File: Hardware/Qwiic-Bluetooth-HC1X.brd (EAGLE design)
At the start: 25.4 x 25.4 mm, 55 parts, among them J1 ISP, J2 Qwiic-L, J3 Qwiic-R, J4 I2C, J5 PIO, U1 ATTiny85-Arduino, U2 HM-17

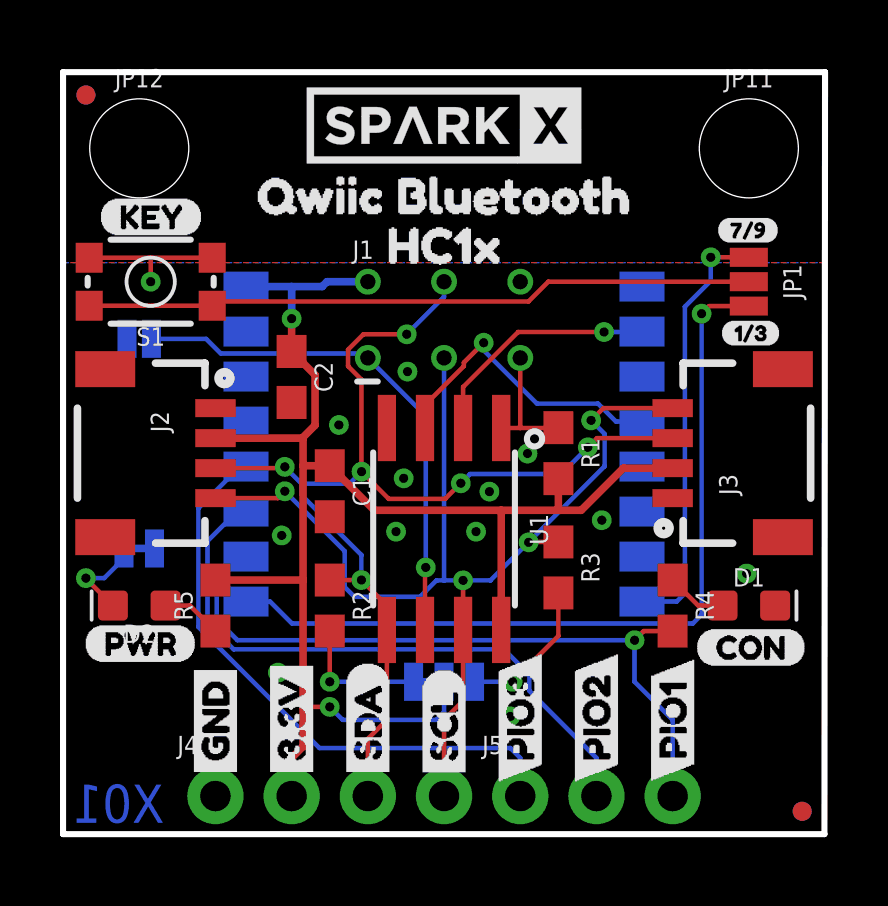
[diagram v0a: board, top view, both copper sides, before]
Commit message: Adding decoupling, fixing silk.
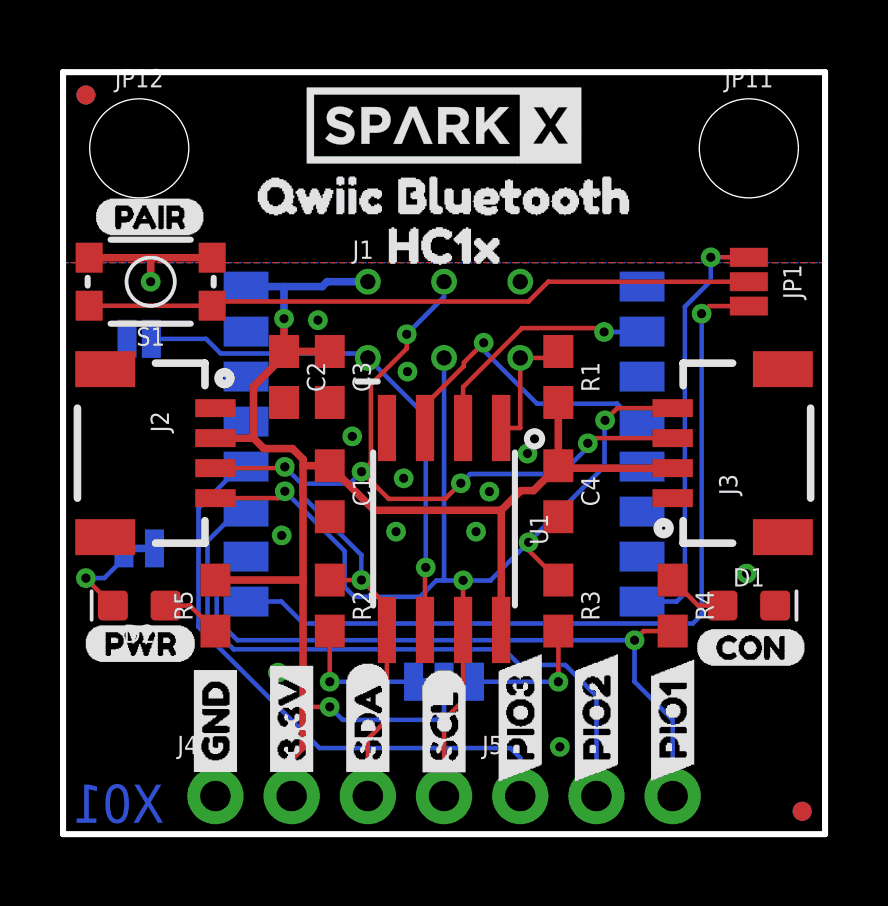
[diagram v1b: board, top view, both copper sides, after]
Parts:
- removed U$12: (no value), Qwiic-Bluetooth-HC1x:KEY6
- removed U$24: (no value), Qwiic-Bluetooth-HC1x:7#915
- added C3: 4.7uF, SparkFun-Capacitors:0603
- added C4: 10uF, SparkFun-Capacitors:0603
- JP3: value (none) -> I2C; device SparkFun-Jumpers:SMT-JUMPER_3_2-NC_TRACE_SILK -> SparkFun-Jumpers:SMT-JUMPER_3_2-NC_TRACE_NO-SILK
- JP4: device SparkFun-Jumpers:SMT-JUMPER_2_NC_TRACE_SILK -> SparkFun-Jumpers:SMT-JUMPER_2_NC_TRACE_NO-SILK
- U$23: device Qwiic-Bluetooth-HC1x:1#314 -> Qwiic-Bluetooth-HC1x:PAIR15
- moved U$23 21.2 mm to (1.02, 20.6)
- moved R1 2.54 mm to (16.5, 15.2)
- moved R3 1.27 mm to (16.5, 7.62)
- moved LOGO2 0.46 mm to (22.9, 12.7), turned to 90 degrees
- moved U$13 0.38 mm to (4.38, 8.13)
- moved U$20 0.38 mm to (14.2, 3.68)
- moved C2 0.25 mm to (7.37, 15.2)
- moved U$19 0.13 mm to (4.38, 15.1)
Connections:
- net PIO1 renamed PIO1/LED
- net 3.3V: now also C3.1, C4.1
- net GND: now also C3.2, C4.2
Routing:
- net 3.3V: track 53.0 -> 54.7 mm
- net SDA: track 39.5 -> 38.3 mm
- net PIO2: track 20.8 -> 21.7 mm

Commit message: Fixing HM-17 pinout, and revising layout to x02
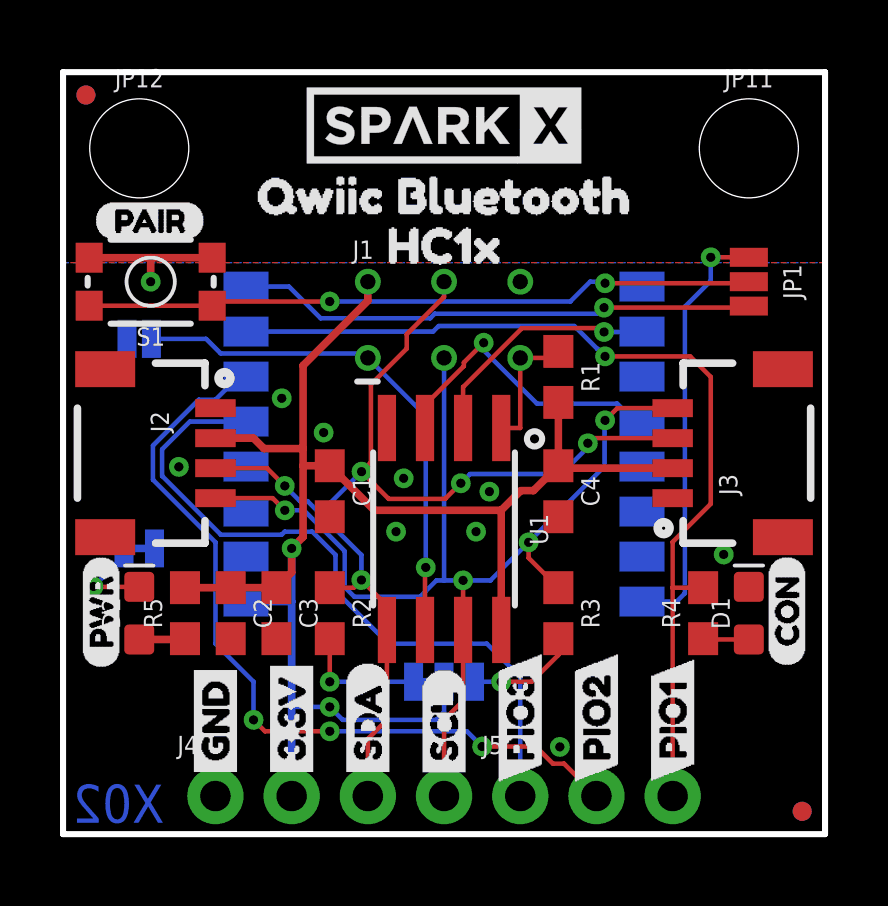
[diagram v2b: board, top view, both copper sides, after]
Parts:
- LOGO2: value SPARKX-LOGO3 -> SPARKX-LOGO4; device SparkX:SPARKX-SMALL -> SparkX:SPARKX-MEDIUM
- moved C3 8.07 mm to (7.11, 7.37)
- moved C2 8.07 mm to (5.59, 7.37)
- moved U$17 3.11 mm to (24.1, 5.59), turned to 90 degrees
- moved R5 1.05 mm to (4.06, 7.37)
- moved R4 1.05 mm to (21.3, 7.37), turned to 90 degrees
- moved U$16 1.00 mm to (1.27, 5.52), turned to 90 degrees
- moved D1 0.25 mm to (22.9, 7.37), turned to 90 degrees
- moved D2 0.25 mm to (2.54, 7.37), turned to 90 degrees
- moved R2 0.25 mm to (8.89, 7.37)
- moved R3 0.25 mm to (16.5, 7.37)
- moved U$23 0.13 mm to (1.02, 20.4)
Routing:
- net PIO0/KEY-HM11: track 27.3 -> 17.4 mm
- net PIO1/LED: track 24.0 -> 31.8 mm
- net PIO2: track 21.7 -> 27.1 mm, vias 0 -> 3
- net PIO3: track 19.9 -> 23.5 mm
- net SCL_PU1: track 4.48 -> 3.71 mm
- net SDA: track 38.3 -> 38.0 mm, vias 6 -> 5
- net N$4: track 22.3 -> 22.4 mm, vias 0 -> 2
- net GND: vias 13 -> 10
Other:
- board text added: "X02"
- board text removed: "X01"
